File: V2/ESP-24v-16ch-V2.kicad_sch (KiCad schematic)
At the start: 6 parts, among them J3 Conn_01x08, J4 Conn_01x08, J5 Conn_01x08, J5 VIN, J6 Conn_01x08, J6 USB

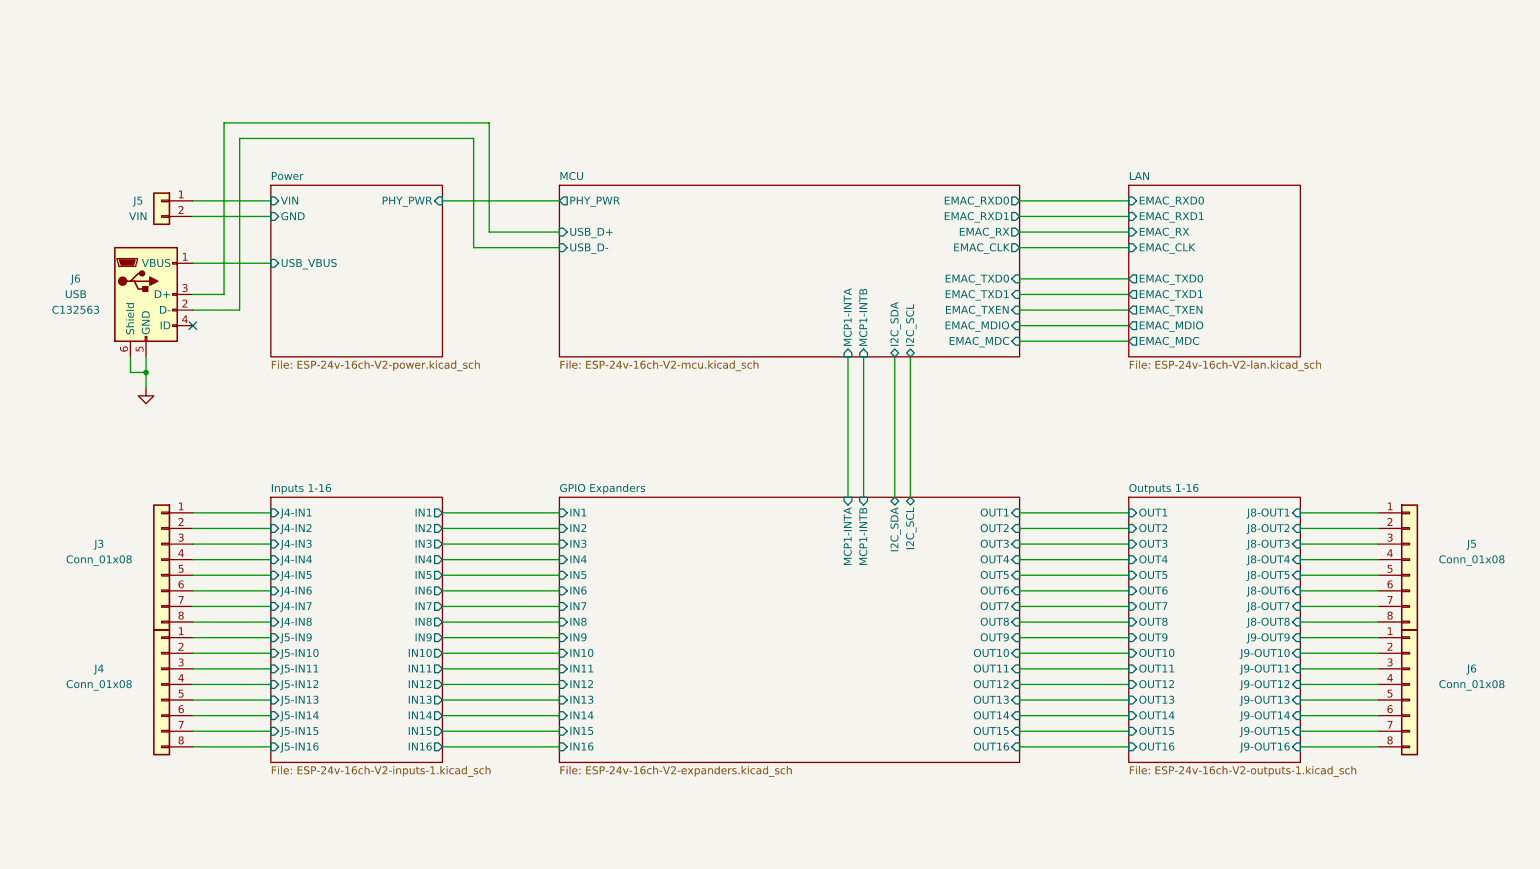
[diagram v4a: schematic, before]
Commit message: Upgrade USB-Micro-B to Type-C connector.
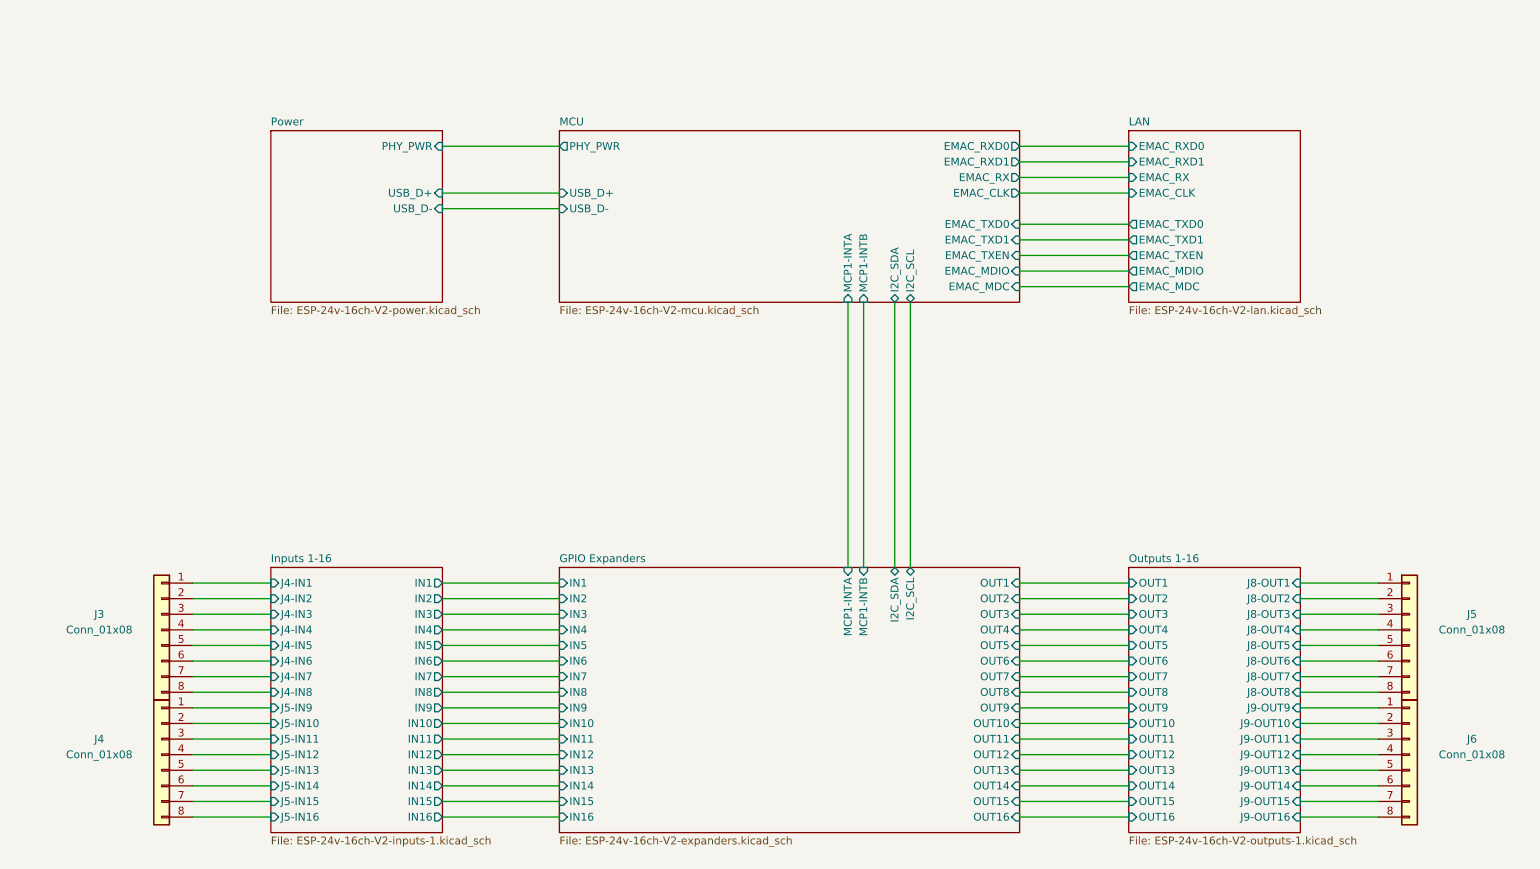
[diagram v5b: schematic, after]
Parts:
- removed J5: VIN, Tales:TerminalBlock_Phoenix_MKDS-3-2-5.08_1x02_P5.08mm_Horizontal, symbol Connector_Generic:Conn_01x02
- removed J6: USB, Tales:USB_Micro-B_Amphenol_10104110_Horizontal, symbol Connector:USB_B_Micro
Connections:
- no-connect marks 1 -> 0
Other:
- sheet Power ports: added USB_D+, USB_D-; removed GND, USB_VBUS, VIN
- moved on the sheet: J3, J4, J5, J6

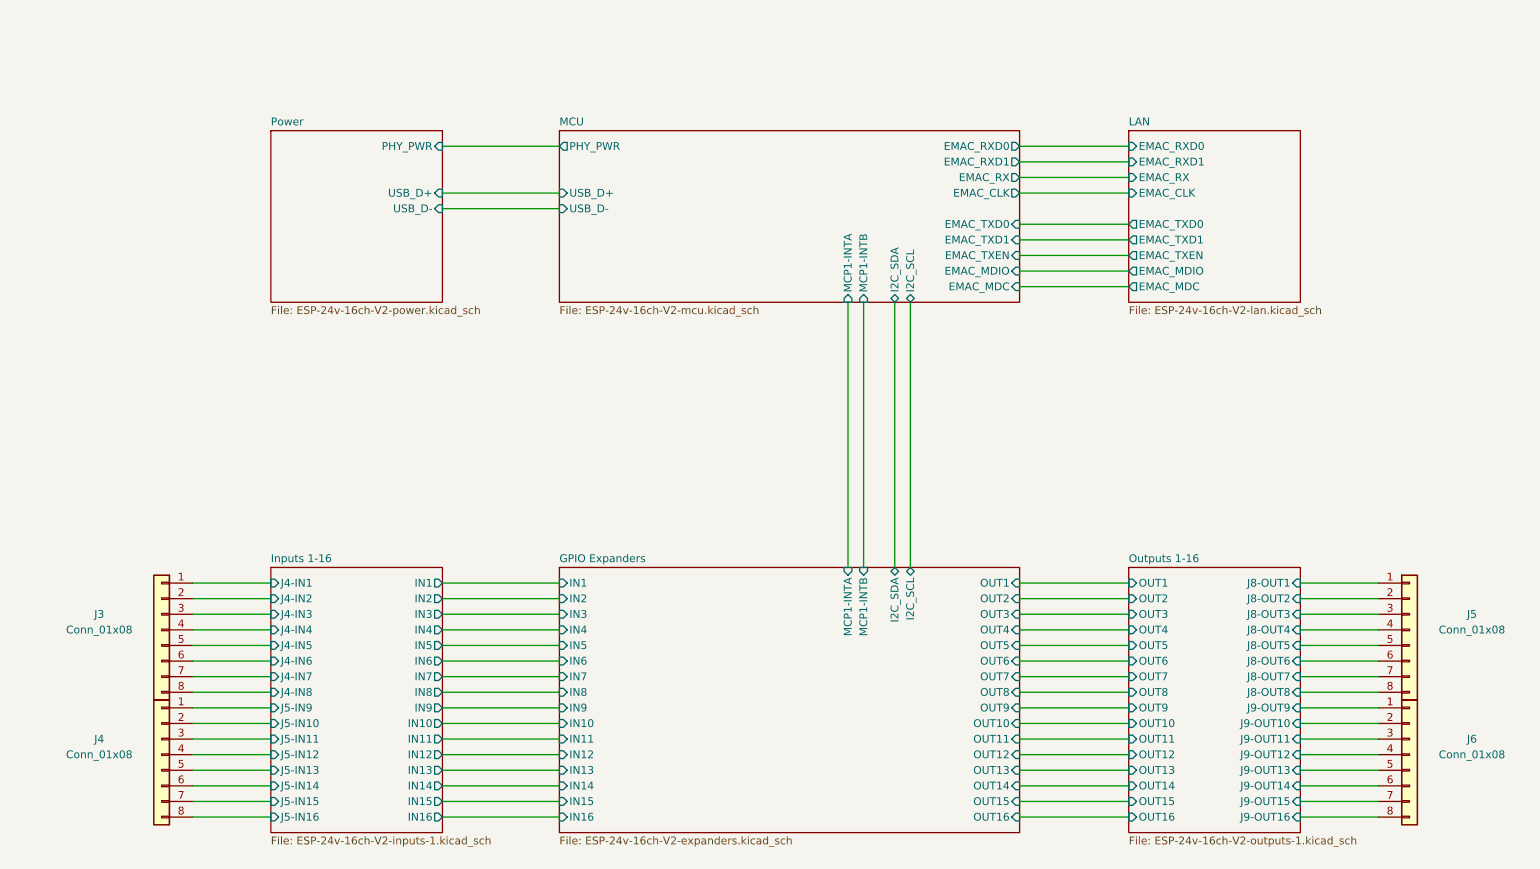
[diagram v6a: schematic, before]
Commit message: Added GPIO and templates info in the schematics
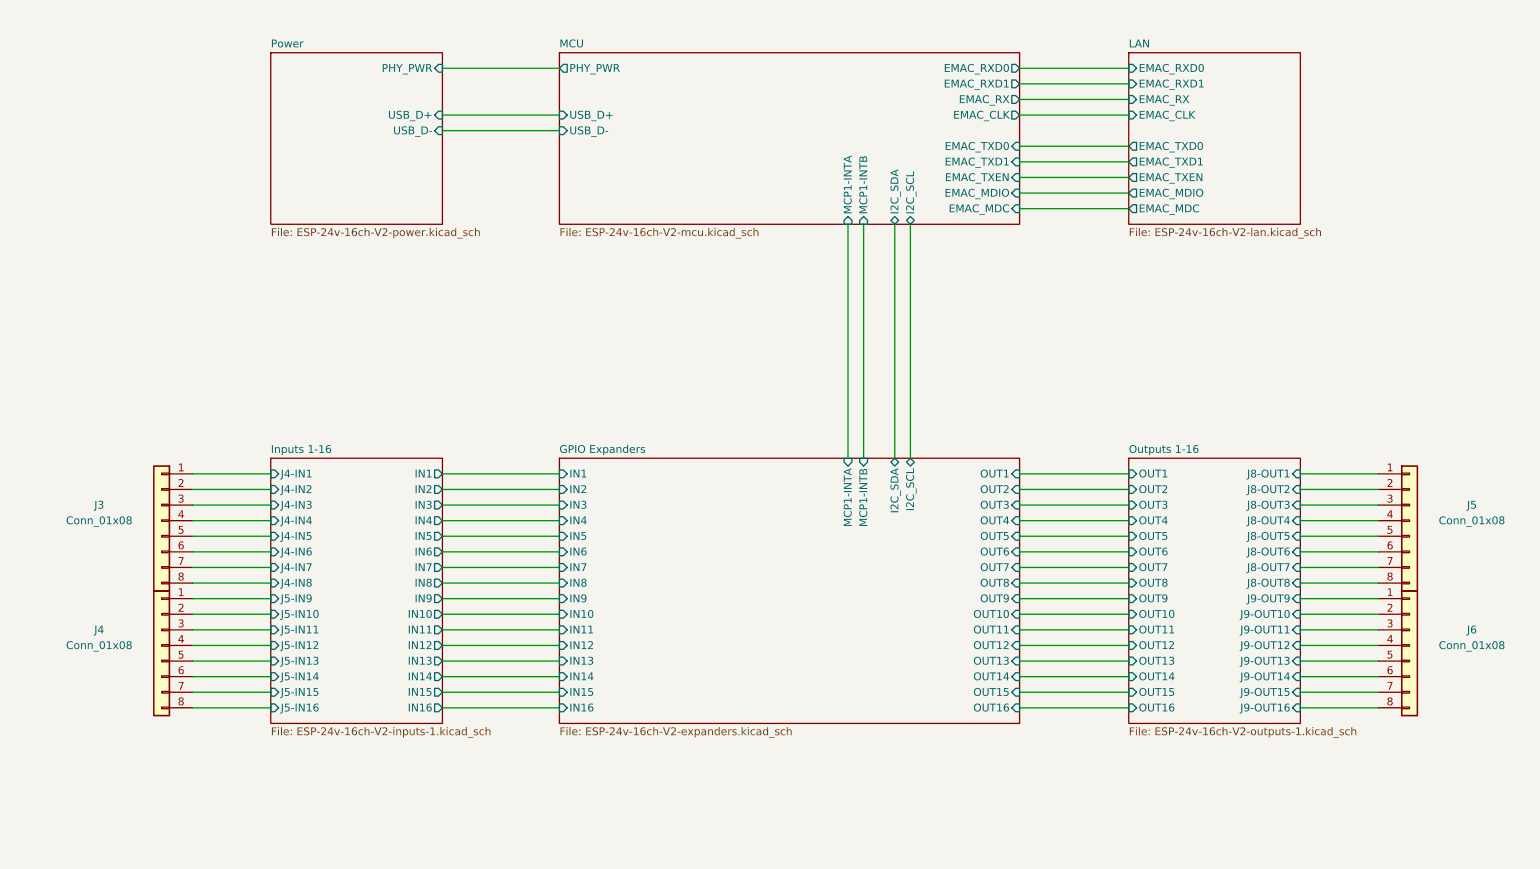
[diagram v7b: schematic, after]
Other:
- moved on the sheet: J3, J4, J5, J6
